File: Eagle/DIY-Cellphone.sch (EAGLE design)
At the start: 69 parts, among them IC1 MEGA1284, J1 ISP, U1 MCP73831, U7 M10_HDWITHOUT_EXCLUSION, X1 BU-SMA-V, X3 CCM03-3002 R102

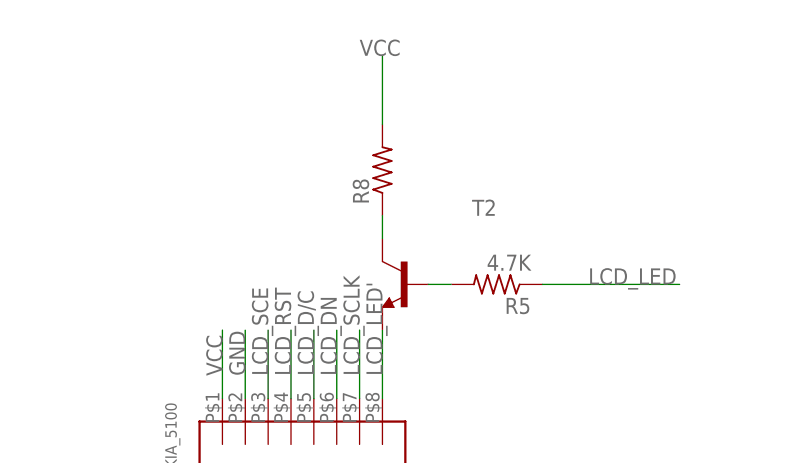
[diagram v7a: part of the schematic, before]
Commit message: Add value (100 ohms) to resistor on LED backlight for the display.
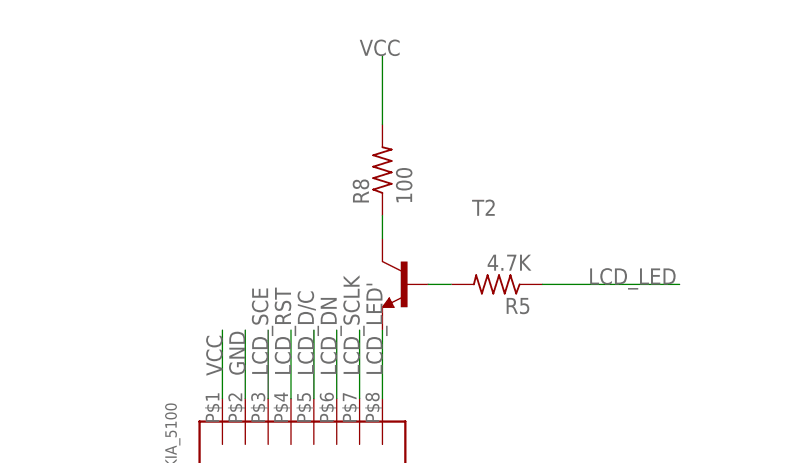
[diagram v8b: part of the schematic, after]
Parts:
- R8: value (none) -> 100
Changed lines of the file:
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@@
 <part name="T2" library="transistor" deviceset="*-NPN-" device="SOT23-BEC" technology="MMBT3904LT1"/>
 <part name="R5" library="rcl" deviceset="R-US_" device="R1206" value="4.7K"/>
-<part name="R8" library="rcl" deviceset="R-US_" device="R1206"/>
+<part name="R8" library="rcl" deviceset="R-US_" device="R1206" value="100"/>
 <part name="U$4" library="cellphone" deviceset="SUPERCAP" device="PAS"/>
 <part name="8MHZ" library="fab" deviceset="CRYSTAL" device=""/>
